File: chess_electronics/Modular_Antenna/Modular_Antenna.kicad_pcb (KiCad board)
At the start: 2 copper layers, 23 x 89.5 mm, 11 parts, among them J1 Screw_Terminal_01x16, J2 Conn_02x04_Counter_Clockwise, U1 SN74LV4051AN

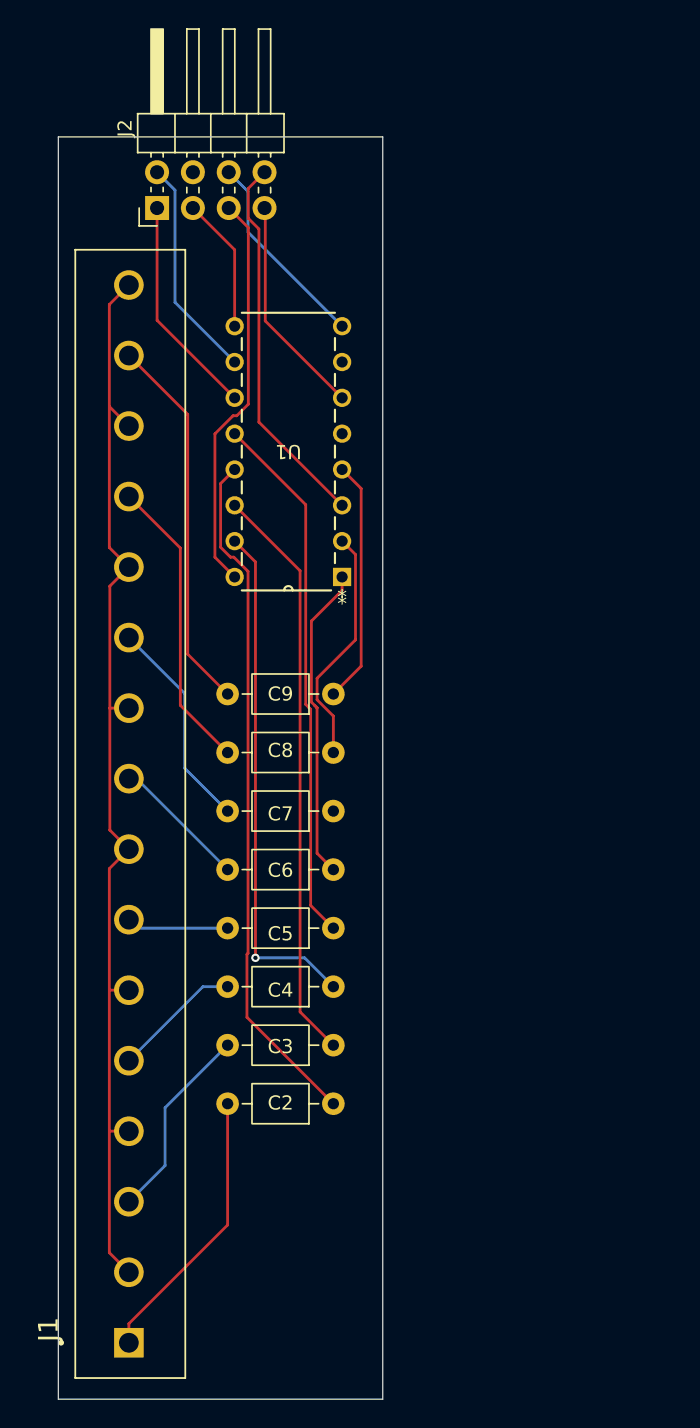
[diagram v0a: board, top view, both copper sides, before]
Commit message: Add normally closed relay to modular antenna design
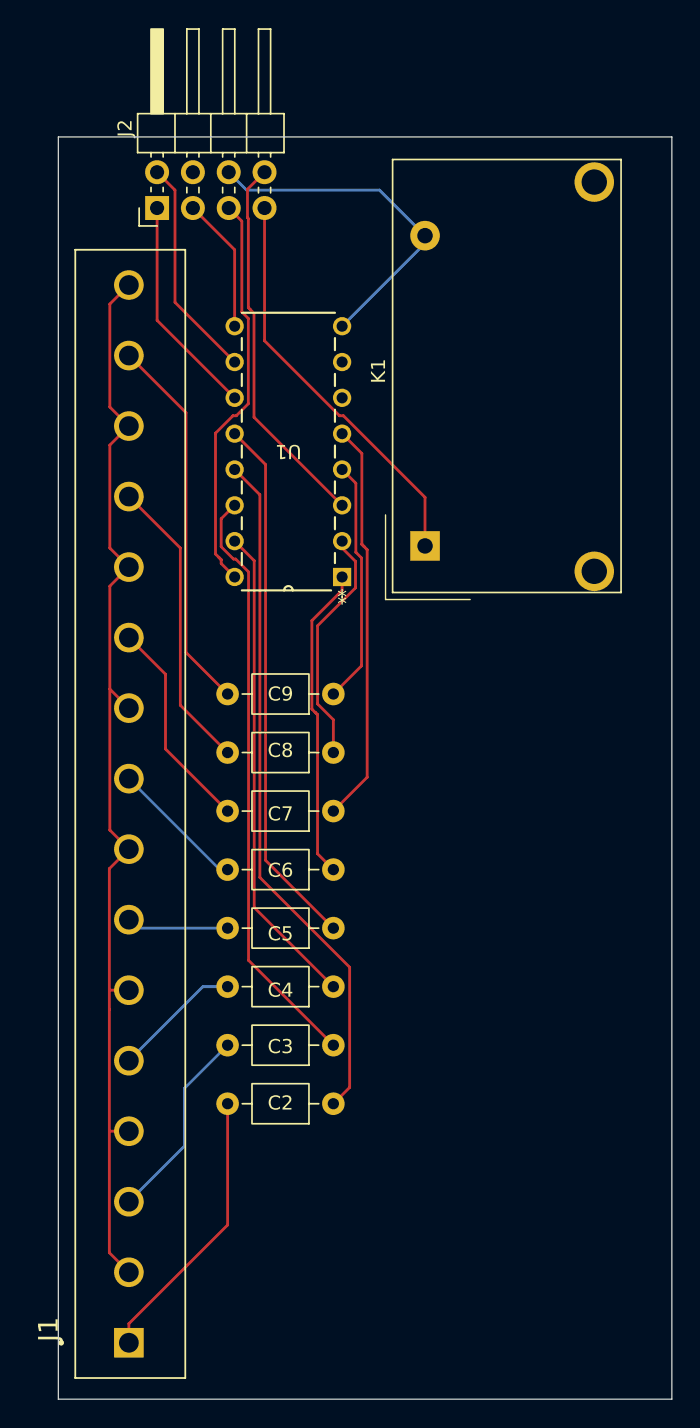
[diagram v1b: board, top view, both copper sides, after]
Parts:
- added K1: Relay_SPST-NC, Relay_THT:Relay_SPST_Zettler-AZSR131, F.Cu at (201.0, 72.5)
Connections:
- U1 pad 6: Net-(J2-Pin_7) -> Net-(U1-INH)
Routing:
- net Net-(U1-Y5): track 0.00 -> 28.7 mm
- net Net-(J2-Pin_7): track 15.7 -> 28.8 mm
- net Net-(J2-Pin_6): track 14.3 -> 24.6 mm
- net Net-(U1-Y2): track 36.5 -> 34.5 mm, vias 1 -> 0
- net Net-(U1-Y1): track 41.2 -> 42.1 mm
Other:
- board size 23 x 89.5 mm -> 43.5 x 89.5 mm
